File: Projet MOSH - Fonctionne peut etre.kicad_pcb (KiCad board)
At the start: 2 copper layers, 68.6 x 53.3 mm, 23 parts, among them J1 Power, J2 Digital/PWM, J3 Analog, J4 Digital/PWM, U2 LTC1050, U4 MCP41100

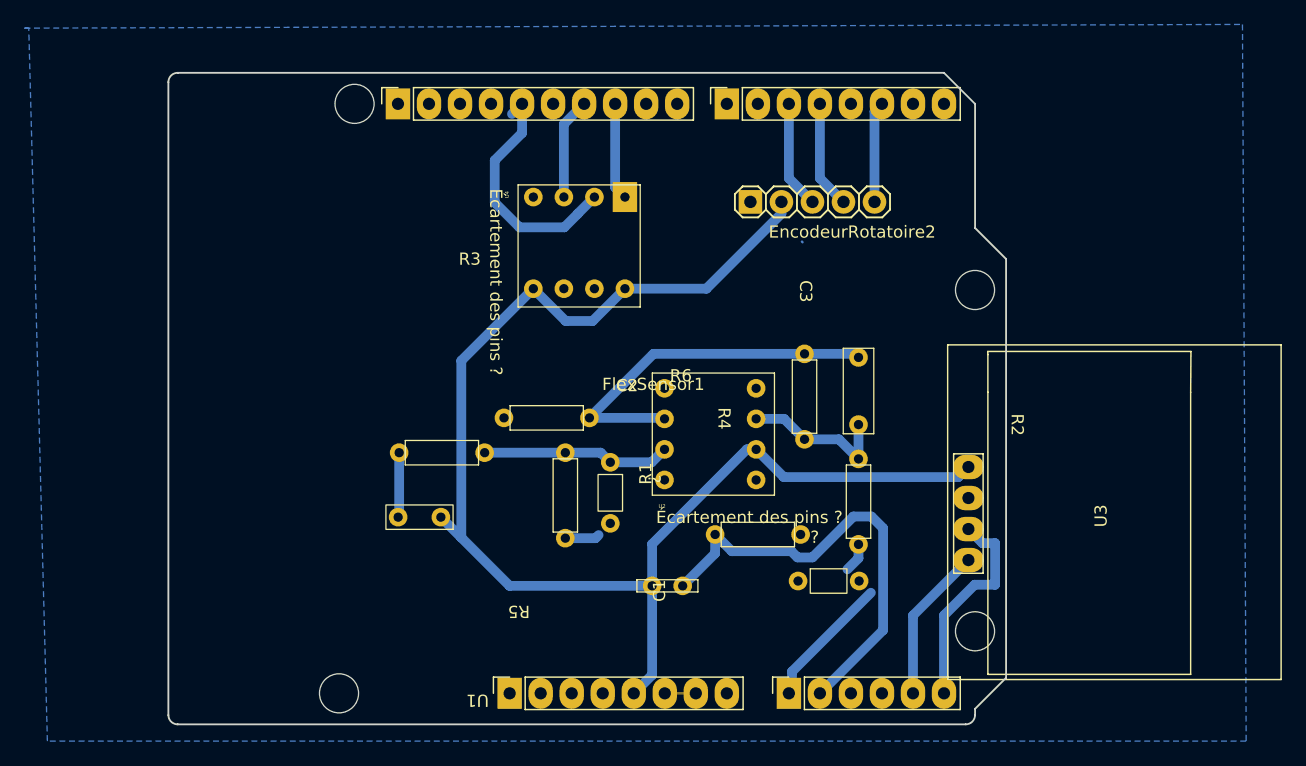
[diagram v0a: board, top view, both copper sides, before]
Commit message: Fonctionne presque ! Juste deux zones GND à connecter et ce sera bon
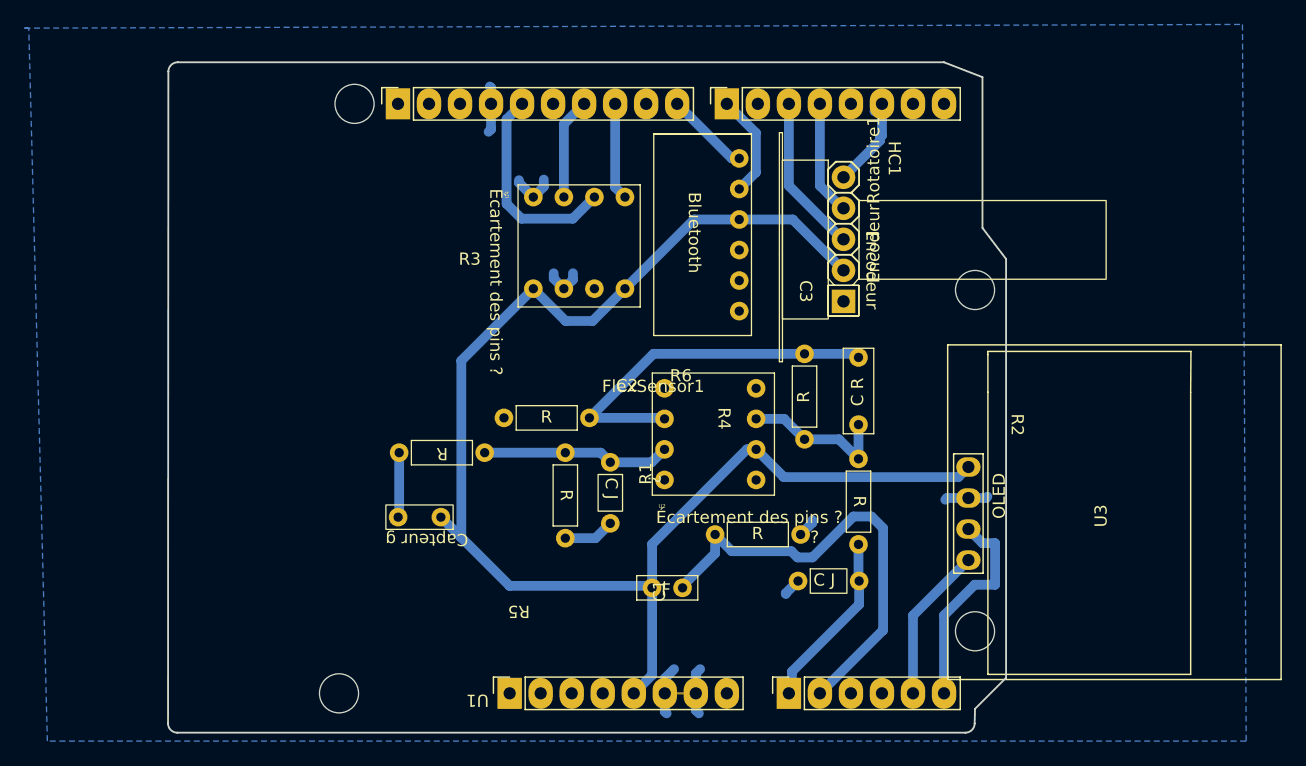
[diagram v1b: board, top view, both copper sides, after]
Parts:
- removed EncodeurRotatoire2: ~, MOSH_empreintes:KY-040
- added EncodeurRotatoire1: ~, MOSH_empreintes:KY-040, F.Cu at (155.3, 61.6)
- added HC1: ~, MOSH_empreintes:Bluetooth HC-05, F.Cu at (146.7, 53.7)
- moved FlexSensor1 0.16 mm to (139.6, 88.8)
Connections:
- net +3.3V renamed +3V3
- J2 pad 1: A5 -> unconnected-(J2-Pin_1-Pad1)
- J2 pad 2: A4 -> unconnected-(J2-Pin_2-Pad2)
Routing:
- net GND: track 5.88 -> 32.3 mm
- net D7: track 0.00 -> 8.52 mm
- net D8: track 0.00 -> 6.93 mm
- net +5V: track 111.7 -> 117.3 mm
- net D5: track 8.83 -> 13.0 mm
- net D13: track 20.2 -> 17.1 mm
- net A0: track 13.4 -> 14.6 mm
- net D4: track 8.83 -> 9.36 mm
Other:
- board size 68.6 x 53.3 mm -> 68.6 x 54.9 mm

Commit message: Wow
It is workiiiiiing
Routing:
- net GND: track 32.3 -> 36.9 mm, vias 0 -> 2
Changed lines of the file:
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@@
   )
   (segment (start 140.64 97.46) (end 143.18 97.46) (width 0.2) (layer "F.Cu") (net 1))
+  (via (at 122.7584 53.264) (size 2) (drill 0.8) (layers "F.Cu" "B.Cu") (free) (net 1))
+  (via (at 129.972 53.1624) (size 2) (drill 0.8) (layers "F.Cu" "B.Cu") (free) (net 1))
   (segment (start 150.546 89.2704) (end 150.546 89.332) (width 0.8) (layer "B.Cu") (net 1))
   (segment (start 143.18 97.46) (end 143.18 95.8344) (width 0.8) (layer "B.Cu") (net 1))
@@
   (segment (start 126.416 49.2) (end 126.416 51.2828) (width 0.8) (layer "B.Cu") (net 1))
   (segment (start 132.4974 84.7586) (end 134.9664 84.7586) (width 0.8) (layer "B.Cu") (net 1))
+  (segment (start 129.972 52.3496) (end 129.972 53.1624) (width 0.8) (layer "B.Cu") (net 1))
+  (segment (start 122.6568 53.3656) (end 122.6568 54.2292) (width 0.8) (layer "B.Cu") (net 1))
   (segment (start 140.64 96.2408) (end 141.402 95.4788) (width 0.8) (layer "B.Cu") (net 1))
   (segment (start 140.64 98.9476) (end 140.7924 99.1) (width 0.8) (layer "B.Cu") (net 1))
@@
   (segment (start 143.18 97.46) (end 143.18 98.846) (width 0.8) (layer "B.Cu") (net 1))
   (segment (start 126.416 47.8792) (end 126.3144 47.7776) (width 0.8) (layer "B.Cu") (net 1))
+  (segment (start 129.8196 52.1972) (end 129.972 52.3496) (width 0.8) (layer "B.Cu") (net 1))
   (segment (start 152.7304 83.4848) (end 152.7304 83.2868) (width 0.8) (layer "B.Cu") (net 1))
   (segment (start 151.76 84.4552) (end 152.7304 83.4848) (width 0.8) (layer "B.Cu") (net 1))
+  (segment (start 129.972 53.1624) (end 129.972 54.0768) (width 0.8) (layer "B.Cu") (net 1))
+  (segment (start 122.7584 53.264) (end 122.6568 53.3656) (width 0.8) (layer "B.Cu") (net 1))
   (segment (start 140.64 97.46) (end 140.64 98.9476) (width 0.8) (layer "B.Cu") (net 1))
   (segment (start 142.87 97.15) (end 143.18 97.46) (width 0.2) (layer "B.Cu") (net 1))
@@
   (segment (start 163.7408 81.4712) (end 163.6016 81.6104) (width 0.8) (layer "B.Cu") (net 1))
   (segment (start 130.734 55.9756) (end 130.734 55.3976) (width 0.8) (layer "B.Cu") (net 1))
+  (segment (start 122.7584 53.264) (end 122.7584 52.502) (width 0.8) (layer "B.Cu") (net 1))
+  (segment (start 122.7584 52.502) (end 123.2156 52.0448) (width 0.8) (layer "B.Cu") (net 1))
   (segment (start 129.878 56.8316) (end 130.734 55.9756) (width 0.8) (layer "B.Cu") (net 1))
   (segment (start 151.5512 88.2652) (end 150.546 89.2704) (width 0.8) (layer "B.Cu") (net 1))
@@
   (segment (start 143.18 95.8344) (end 143.5356 95.4788) (width 0.8) (layer "B.Cu") (net 1))
   (segment (start 126.416 49.2) (end 126.416 47.8792) (width 0.8) (layer "B.Cu") (net 1))
+  (segment (start 129.972 54.0768) (end 129.8196 54.2292) (width 0.8) (layer "B.Cu") (net 1))
   (segment (start 146.736 58.6672) (end 143.0424 58.6672) (width 0.8) (layer "B.Cu") (net 3))
   (segment (start 146.736 58.6672) (end 151.1108 58.6672) (width 0.8) (layer "B.Cu") (net 3))

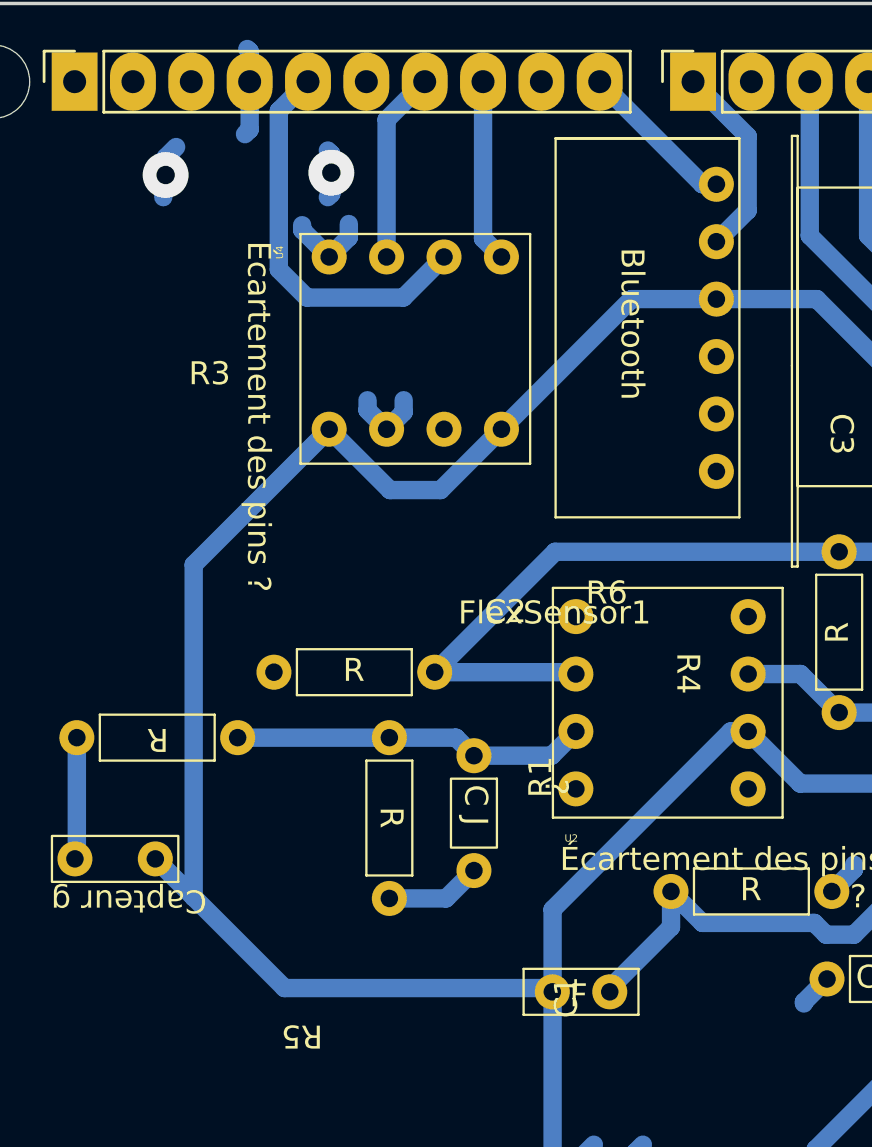
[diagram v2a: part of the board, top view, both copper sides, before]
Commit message: Il manque a relier les vias
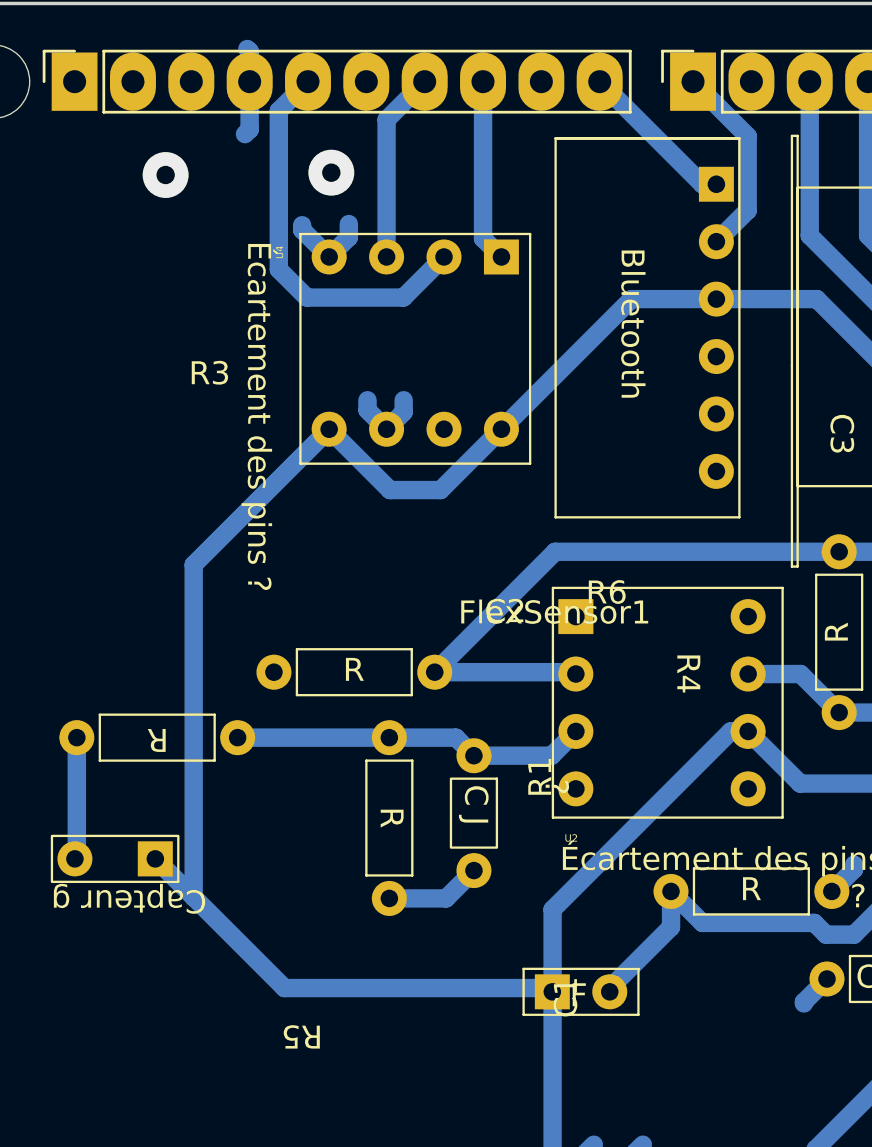
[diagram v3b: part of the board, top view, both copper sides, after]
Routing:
- net GND: track 36.9 -> 32.5 mm
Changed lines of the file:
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@@
     (fp_line (start 10 0) (end 0 0)
       (stroke (width 0.1) (type default)) (layer "F.SilkS"))
-    (pad "1" thru_hole circle (at 1 -8.75) (size 1.524 1.524) (drill 0.762) (layers "*.Cu" "*.Mask")
+    (pad "1" thru_hole rect (at 1 -8.75) (size 1.524 1.524) (drill 0.762) (layers "*.Cu" "*.Mask")
       (net 32 "unconnected-(U2-NC_2-Pad1)") (pinfunction "NC_2") (pintype "no_connect"))
     (pad "2" thru_hole circle (at 1 -6.25) (size 1.524 1.524) (drill 0.762) (layers "*.Cu" "*.Mask")
@@
     (fp_circle (center 0 0) (end 1.7 0)
       (stroke (width 0.05) (type solid)) (fill none) (layer "F.CrtYd"))
-    (pad "" np_thru_hole circle locked (at 0 0) (size 3.2 3.2) (drill 3.2) (layers "*.Cu" "*.Mask"))
+    (pad "" np_thru_hole circle locked (at 0 0) (size 3.2 3.2) (drill 3.2) (layers "F&B.Cu" "*.Mask" "Eco1.User"))
   )
   (footprint "MOSH_empreintes:LTC1050 et MCP" (layer "F.Cu")
@@
     (fp_line (start 10 0) (end 0 0)
       (stroke (width 0.1) (type default)) (layer "F.SilkS"))
-    (pad "1" thru_hole circle (at 1 -8.75 270) (size 1.524 1.524) (drill 0.762) (layers "*.Cu" "*.Mask")
+    (pad "1" thru_hole rect (at 1 -8.75 270) (size 1.524 1.524) (drill 0.762) (layers "*.Cu" "*.Mask")
       (net 22 "D10") (pinfunction "~{CS}") (pintype "input"))
     (pad "2" thru_hole circle (at 1 -6.25 270) (size 1.524 1.524) (drill 0.762) (layers "*.Cu" "*.Mask")
@@
     (fp_rect (start -1 -1) (end 4.5 1)
       (stroke (width 0.1) (type default)) (fill none) (layer "F.SilkS"))
-    (pad "1" thru_hole circle (at 0 0 180) (size 1.524 1.524) (drill 0.762) (layers "*.Cu" "*.Mask")
+    (pad "1" thru_hole rect (at 0 0 180) (size 1.524 1.524) (drill 0.762) (layers "*.Cu" "*.Mask")
       (net 3 "+5V") (pinfunction "5V") (pintype "passive"))
     (pad "2" thru_hole circle (at 3.5 0 180) (size 1.524 1.524) (drill 0.762) (layers "*.Cu" "*.Mask")
@@
     (fp_line (start 3.75 1) (end 3.75 -1)
       (stroke (width 0.1) (type default)) (layer "F.SilkS"))
-    (pad "1" thru_hole circle (at 0 0) (size 1.524 1.524) (drill 0.762) (layers "*.Cu" "*.Mask")
+    (pad "1" thru_hole rect (at 0 0) (size 1.524 1.524) (drill 0.762) (layers "*.Cu" "*.Mask")
       (net 3 "+5V") (pinfunction "1") (pintype "output"))
     (pad "2" thru_hole circle (at 2.5 0) (size 1.524 1.524) (drill 0.762) (layers "*.Cu" "*.Mask")
@@
     (fp_rect (start -2 7) (end -2 -1)
       (stroke (width 0.1) (type default)) (fill none) (layer "F.SilkS"))
-    (pad "1" thru_hole circle (at 0 0 270) (size 1.524 1.524) (drill 0.762) (layers "*.Cu" "*.Mask")
+    (pad "1" thru_hole rect (at 0 0 270) (size 1.524 1.524) (drill 0.762) (layers "*.Cu" "*.Mask")
       (net 14 "D8") (pinfunction "RXD") (pintype "bidirectional"))
     (pad "2" thru_hole circle (at 2.5 0 270) (size 1.524 1.524) (drill 0.762) (layers "*.Cu" "*.Mask")
@@
   (segment (start 126.416 49.2) (end 126.416 51.2828) (width 0.8) (layer "B.Cu") (net 1))
   (segment (start 132.4974 84.7586) (end 134.9664 84.7586) (width 0.8) (layer "B.Cu") (net 1))
-  (segment (start 129.972 52.3496) (end 129.972 53.1624) (width 0.8) (layer "B.Cu") (net 1))
-  (segment (start 122.6568 53.3656) (end 122.6568 54.2292) (width 0.8) (layer "B.Cu") (net 1))
   (segment (start 140.64 96.2408) (end 141.402 95.4788) (width 0.8) (layer "B.Cu") (net 1))
   (segment (start 140.64 98.9476) (end 140.7924 99.1) (width 0.8) (layer "B.Cu") (net 1))
@@
   (segment (start 143.18 97.46) (end 143.18 98.846) (width 0.8) (layer "B.Cu") (net 1))
   (segment (start 126.416 47.8792) (end 126.3144 47.7776) (width 0.8) (layer "B.Cu") (net 1))
-  (segment (start 129.8196 52.1972) (end 129.972 52.3496) (width 0.8) (layer "B.Cu") (net 1))
   (segment (start 152.7304 83.4848) (end 152.7304 83.2868) (width 0.8) (layer "B.Cu") (net 1))
   (segment (start 151.76 84.4552) (end 152.7304 83.4848) (width 0.8) (layer "B.Cu") (net 1))
-  (segment (start 129.972 53.1624) (end 129.972 54.0768) (width 0.8) (layer "B.Cu") (net 1))
   (segment (start 122.7584 53.264) (end 122.6568 53.3656) (width 0.8) (layer "B.Cu") (net 1))
   (segment (start 140.64 97.46) (end 140.64 98.9476) (width 0.8) (layer "B.Cu") (net 1))
@@
   (segment (start 163.7408 81.4712) (end 163.6016 81.6104) (width 0.8) (layer "B.Cu") (net 1))
   (segment (start 130.734 55.9756) (end 130.734 55.3976) (width 0.8) (layer "B.Cu") (net 1))
-  (segment (start 122.7584 53.264) (end 122.7584 52.502) (width 0.8) (layer "B.Cu") (net 1))
-  (segment (start 122.7584 52.502) (end 123.2156 52.0448) (width 0.8) (layer "B.Cu") (net 1))
   (segment (start 129.878 56.8316) (end 130.734 55.9756) (width 0.8) (layer "B.Cu") (net 1))
   (segment (start 151.5512 88.2652) (end 150.546 89.2704) (width 0.8) (layer "B.Cu") (net 1))
@@
   (segment (start 143.18 95.8344) (end 143.5356 95.4788) (width 0.8) (layer "B.Cu") (net 1))
   (segment (start 126.416 49.2) (end 126.416 47.8792) (width 0.8) (layer "B.Cu") (net 1))
-  (segment (start 129.972 54.0768) (end 129.8196 54.2292) (width 0.8) (layer "B.Cu") (net 1))
   (segment (start 146.736 58.6672) (end 143.0424 58.6672) (width 0.8) (layer "B.Cu") (net 3))
   (segment (start 146.736 58.6672) (end 151.1108 58.6672) (width 0.8) (layer "B.Cu") (net 3))
